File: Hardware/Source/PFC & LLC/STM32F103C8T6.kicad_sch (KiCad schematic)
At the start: 96 parts, among them J3 Conn_01x06_Socket, J4 Conn_01x02_Socket, J5 Conn_01x04_Pin, J6 Conn_01x05_Socket, Q6 LN2302LT1G, Q7 LN2302LT1G, Q8 LN2302LT1G, Q9 MMBT2222A, SW1 SW_Push, U10 ADS1115IDGS, U11 STM32F103C8T6, U12 MAX485CSA, Y1 Crystal_8MHz_SMD-4PIN

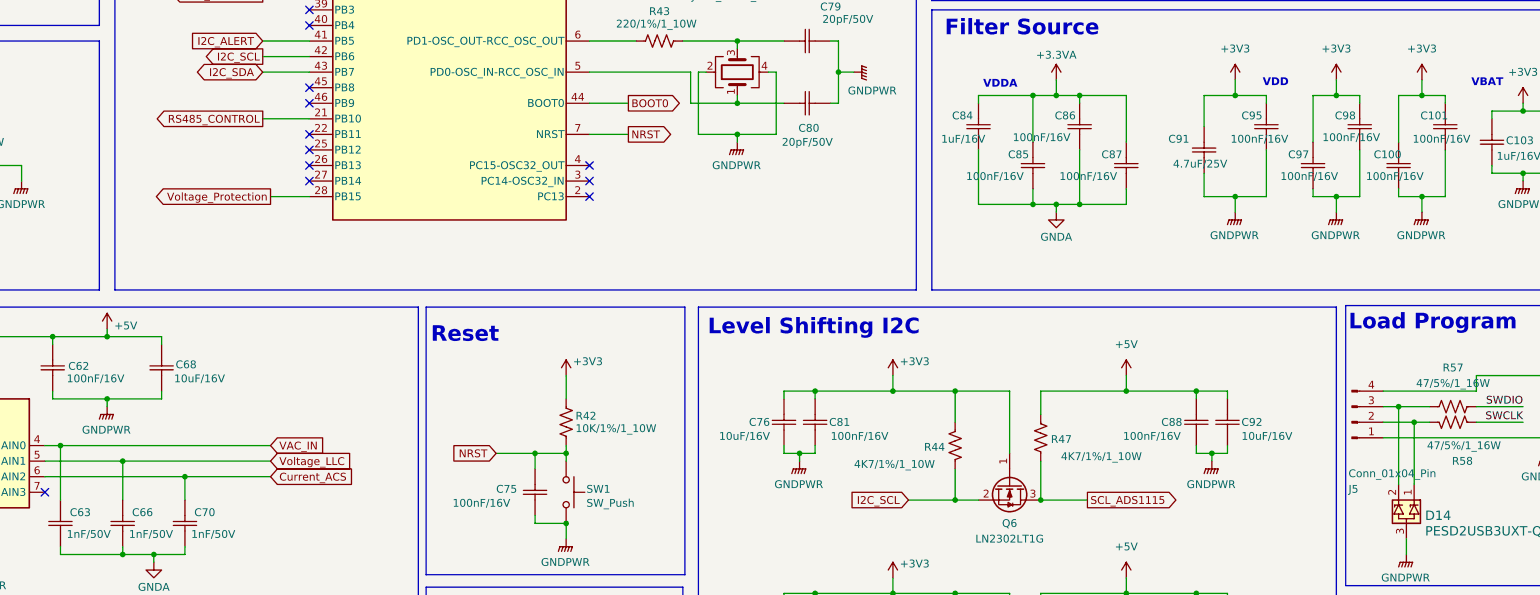
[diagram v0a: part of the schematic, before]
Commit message: Update PFC&LLC
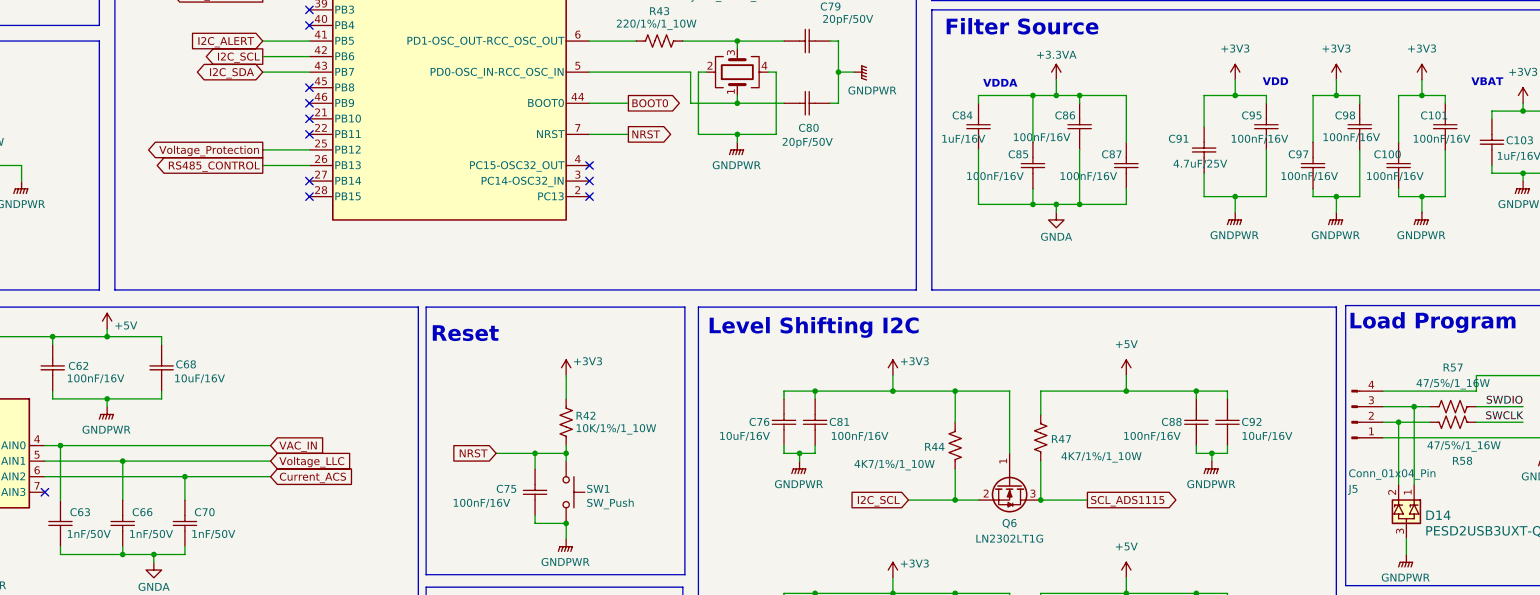
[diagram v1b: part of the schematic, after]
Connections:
- net RS485_CONTROL: now also U11.26 (PB13); no longer U11.21 (PB10)
- net Voltage_Protection: now also U11.25 (PB12); no longer U11.28 (PB15)
- net at J5.2 (Pin_2), R58.1: now also D14.2; no longer D14.1
- net at J5.3 (Pin_3), R57.1: now also D14.1; no longer D14.2
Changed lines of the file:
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@@
 	)
 	(junction
-		(at 293.37 160.02)
+		(at 295.91 160.02)
 		(diameter 0)
 		(color 0 0 0 0)
@@
 	)
 	(junction
+		(at 293.37 162.56)
+		(diameter 0)
+		(color 0 0 0 0)
+	)
+	(junction
 		(at 365.76 121.92)
 		(diameter 0)
@@
 	)
 	(junction
-		(at 295.91 162.56)
-		(diameter 0)
-		(color 0 0 0 0)
-	)
-	(junction
 		(at 307.34 73.66)
 		(diameter 0)
@@
 	)
 	(no_connect
-		(at 115.57 118.11)
-	)
-	(no_connect
-		(at 115.57 120.65)
-	)
-	(no_connect
 		(at 115.57 95.25)
 	)
@@
 	)
 	(no_connect
+		(at 115.57 125.73)
+	)
+	(no_connect
 		(at 115.57 115.57)
 	)
 	(no_connect
+		(at 115.57 113.03)
+	)
+	(no_connect
 		(at 161.29 125.73)
 	)
@@
 	(wire
 		(pts
+			(xy 295.91 160.02) (xy 298.45 160.02)
+		)
+		(stroke
+			(width 0)
+			(type default)
+		)
+	)
+	(wire
+		(pts
 			(xy 241.3 127) (xy 248.92 127)
 		)
@@
 	(wire
 		(pts
-			(xy 293.37 160.02) (xy 293.37 172.72)
+			(xy 260.35 200.66) (xy 260.35 199.39)
 		)
 		(stroke
@@
 	(wire
 		(pts
-			(xy 260.35 200.66) (xy 260.35 199.39)
+			(xy 234.95 232.41) (xy 234.95 238.76)
 		)
 		(stroke
@@
 	(wire
 		(pts
-			(xy 234.95 232.41) (xy 234.95 238.76)
+			(xy 293.37 162.56) (xy 293.37 172.72)
 		)
 		(stroke
@@
 	(wire
 		(pts
+			(xy 293.37 162.56) (xy 298.45 162.56)
+		)
+		(stroke
+			(width 0)
+			(type default)
+		)
+	)
+	(wire
+		(pts
 			(xy 347.98 116.84) (xy 368.3 116.84)
 		)
@@
 	(wire
 		(pts
-			(xy 109.22 125.73) (xy 115.57 125.73)
-		)
-		(stroke
-			(width 0)
-			(type default)
-		)
-	)
-	(wire
-		(pts
 			(xy 360.68 121.92) (xy 360.68 125.73)
 		)
@@
 	(wire
 		(pts
+			(xy 107.95 118.11) (xy 115.57 118.11)
+		)
+		(stroke
+			(width 0)
+			(type default)
+		)
+	)
+	(wire
+		(pts
 			(xy 321.31 40.64) (xy 321.31 45.72)
 		)
@@
 	(wire
 		(pts
+			(xy 295.91 160.02) (xy 295.91 172.72)
+		)
+		(stroke
+			(width 0)
+			(type default)
+		)
+	)
+	(wire
+		(pts
 			(xy 87.63 210.82) (xy 81.28 210.82)
 		)
@@
 	(wire
 		(pts
-			(xy 290.83 162.56) (xy 295.91 162.56)
-		)
-		(stroke
-			(width 0)
-			(type default)
-		)
-	)
-	(wire
-		(pts
 			(xy 363.22 110.49) (xy 363.22 119.38)
 		)
@@
 	(wire
 		(pts
+			(xy 107.95 120.65) (xy 115.57 120.65)
+		)
+		(stroke
+			(width 0)
+			(type default)
+		)
+	)
+	(wire
+		(pts
 			(xy 345.44 53.34) (xy 345.44 67.31)
 		)
@@
 	(wire
 		(pts
-			(xy 290.83 160.02) (xy 293.37 160.02)
+			(xy 290.83 160.02) (xy 295.91 160.02)
 		)
 		(stroke
@@
 	(wire
 		(pts
-			(xy 295.91 162.56) (xy 295.91 172.72)
-		)
-		(stroke
-			(width 0)
-			(type default)
-		)
-	)
-	(wire
-		(pts
 			(xy 107.95 87.63) (xy 115.57 87.63)
 		)
@@
 	(wire
 		(pts
-			(xy 293.37 160.02) (xy 298.45 160.02)
-		)
-		(stroke
-			(width 0)
-			(type default)
-		)
-	)
-	(wire
-		(pts
 			(xy 278.13 55.88) (xy 281.94 55.88)
 		)
@@
 	(wire
 		(pts
-			(xy 107.95 113.03) (xy 115.57 113.03)
-		)
-		(stroke
-			(width 0)
-			(type default)
-		)
-	)
-	(wire
-		(pts
 			(xy 38.1 120.65) (xy 40.64 120.65)
 		)
@@
 	(wire
 		(pts
-			(xy 295.91 162.56) (xy 298.45 162.56)
+			(xy 290.83 162.56) (xy 293.37 162.56)
 		)
 		(stroke
@@
 	(global_label "RS485_CONTROL"
 		(shape output)
-		(at 107.95 113.03 180)
+		(at 107.95 120.65 180)
 		(fields_autoplaced yes)
 		(effects
@@
 		)
 		(property "Intersheetrefs" "${INTERSHEET_REFS}"
-			(at 89.362 113.03 0)
+			(at 89.362 120.65 0)
 			(effects
 				(font
@@
 	(global_label "Voltage_Protection"
 		(shape output)
-		(at 109.22 125.73 180)
+		(at 107.95 118.11 180)
 		(fields_autoplaced yes)
 		(effects
@@
 		)
 		(property "Intersheetrefs" "${INTERSHEET_REFS}"
-			(at 88.5155 125.73 0)
+			(at 87.2455 118.11 0)
 			(effects
 				(font

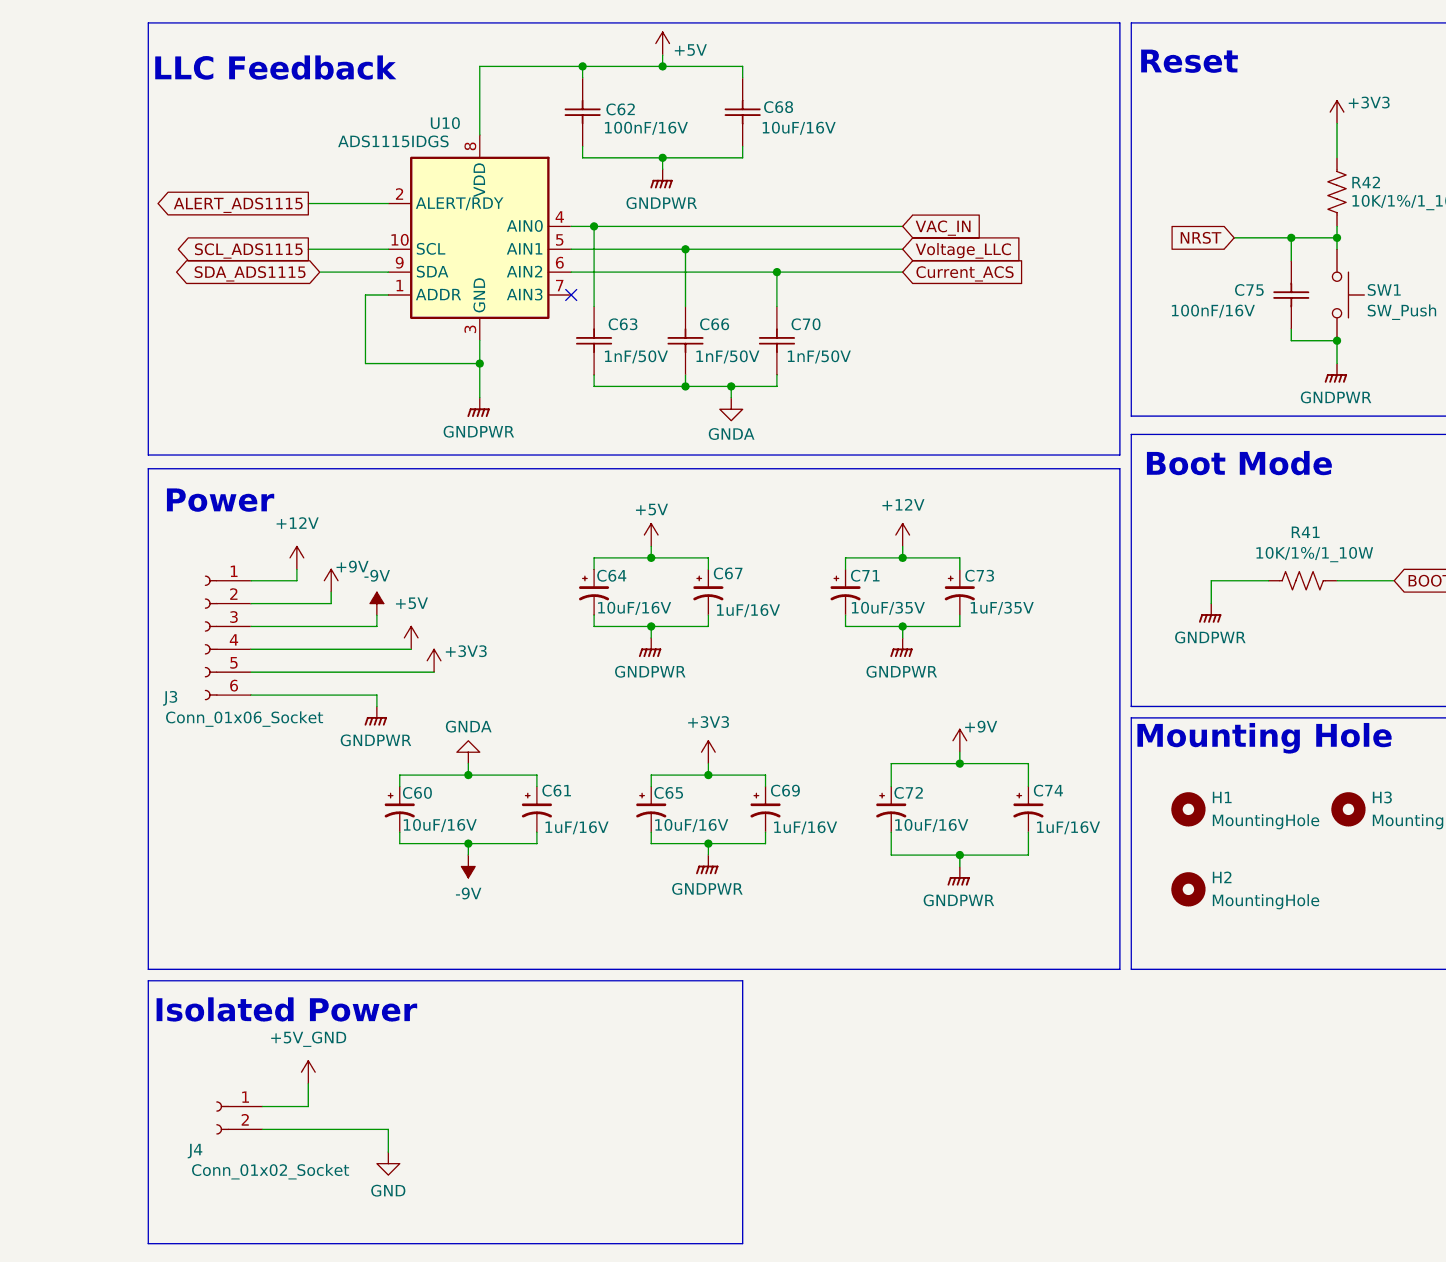
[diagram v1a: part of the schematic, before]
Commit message: Update PFC&LLC
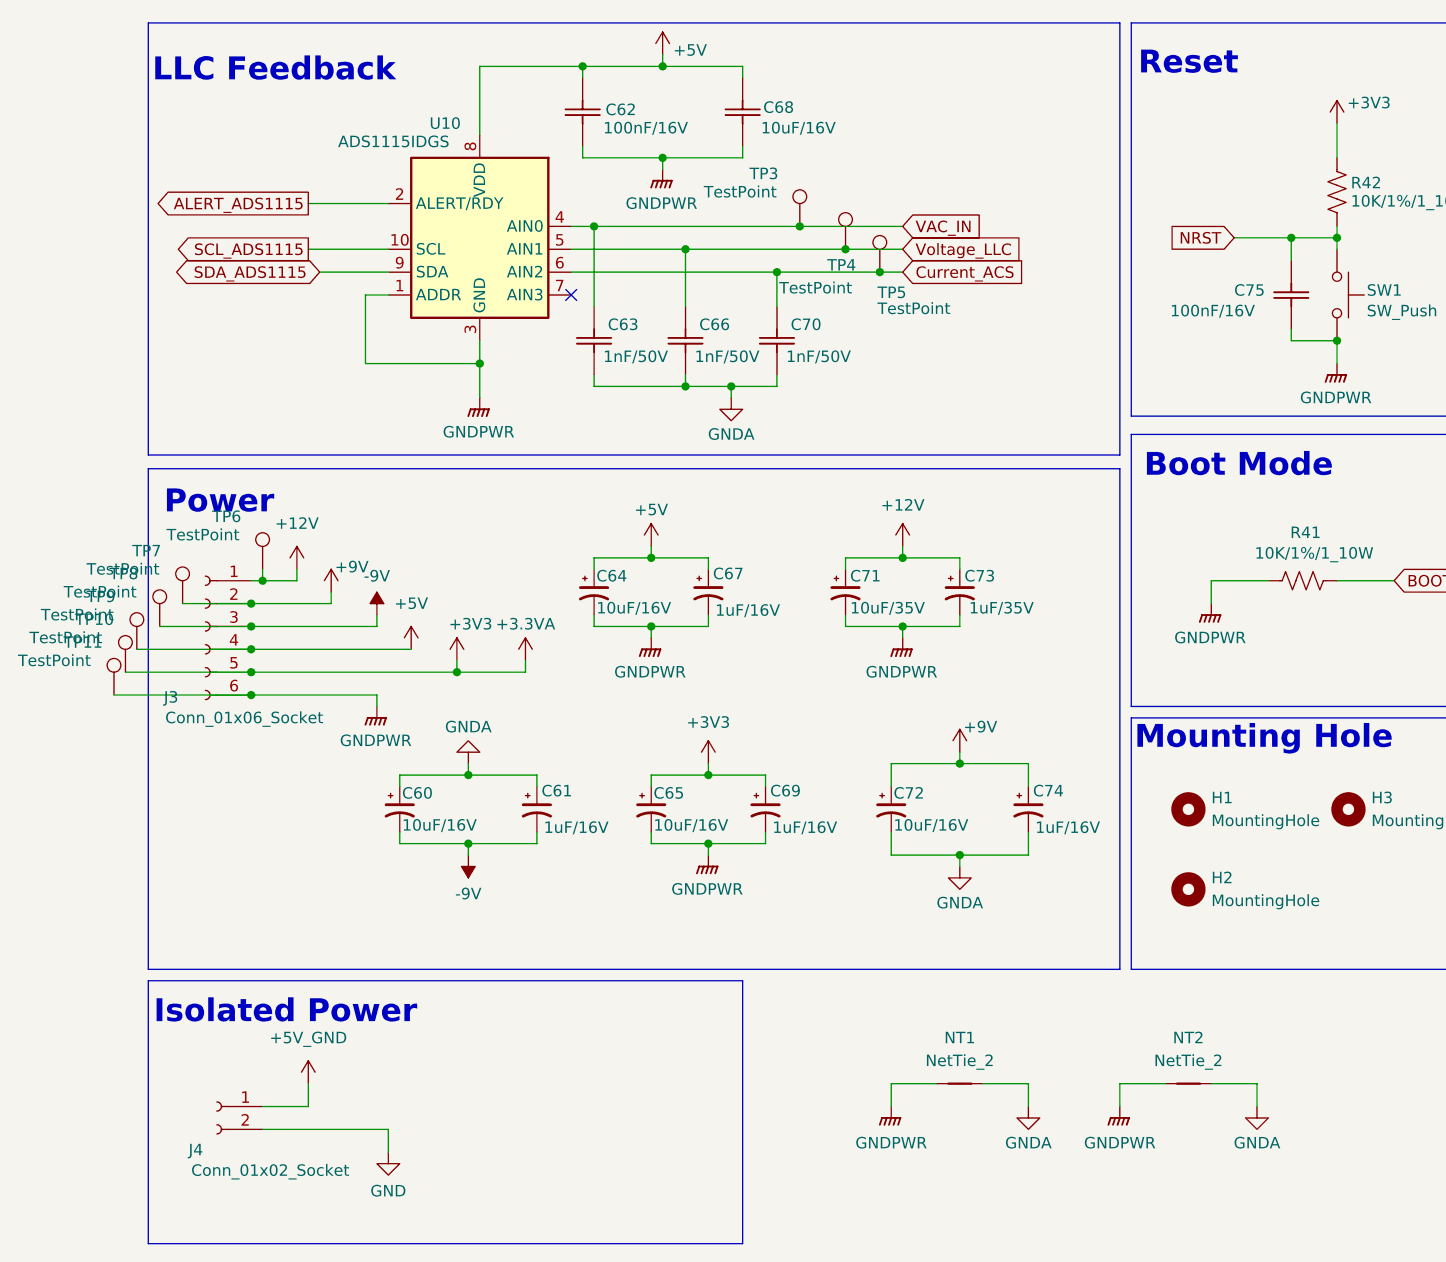
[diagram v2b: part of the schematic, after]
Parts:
- added NT1, NT2: NetTie_2, NetTie:NetTie-2_SMD_Pad0.5mm, symbol Device:NetTie_2
- added TP10, TP11, TP3, TP4, TP5, TP6, TP7, TP8, TP9: TestPoint, TestPoint:TestPoint_Pad_D1.0mm, symbol Connector:TestPoint
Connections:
- net +3V3 is gone; now on net +3.3VA: C100.2, C101.2, C102.2, C103.2, C104.2, C105.2, C65.1, C69.1, C76.2, C77.2, C78.2, C81.2, C82.2, C83.2, C91.2, C95.2, C97.2, C98.2, J3.5 (Pin_5), J5.4 (Pin_4), Q6.1 (G), Q7.1 (G), Q8.1 (G), R42.2, R44.2, R45.2, R46.2, R50.2, R52.1, R53.2, R54.2, R62.2, R63.2, U11.1 (VBAT), U11.24 (VDD_1), U11.36 (VDD_2), U11.48 (VDD_3)
- net +12V: now also TP6.1
- net +3.3VA: now also TP10.1
- net +5V: now also TP9.1
- net +9V: now also TP7.1
- net -9V: now also TP8.1
- net Current_ACS: now also TP5.1
- net GNDA: now also C72.2, C74.2, NT1.2, NT2.2
- net GNDPWR: now also NT1.1, NT2.1, TP11.1; no longer C72.2, C74.2
- net VAC_IN: now also TP3.1
- net Voltage_LLC: now also TP4.1

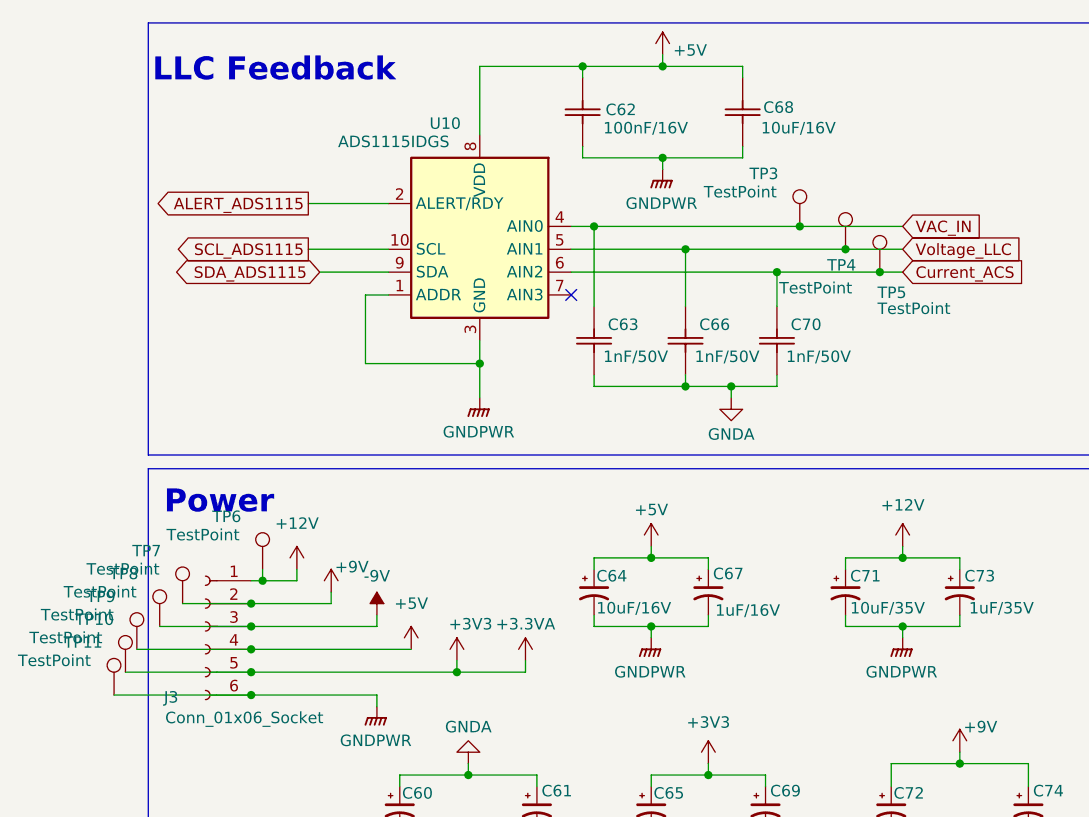
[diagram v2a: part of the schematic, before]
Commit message: Update PFC&LLC
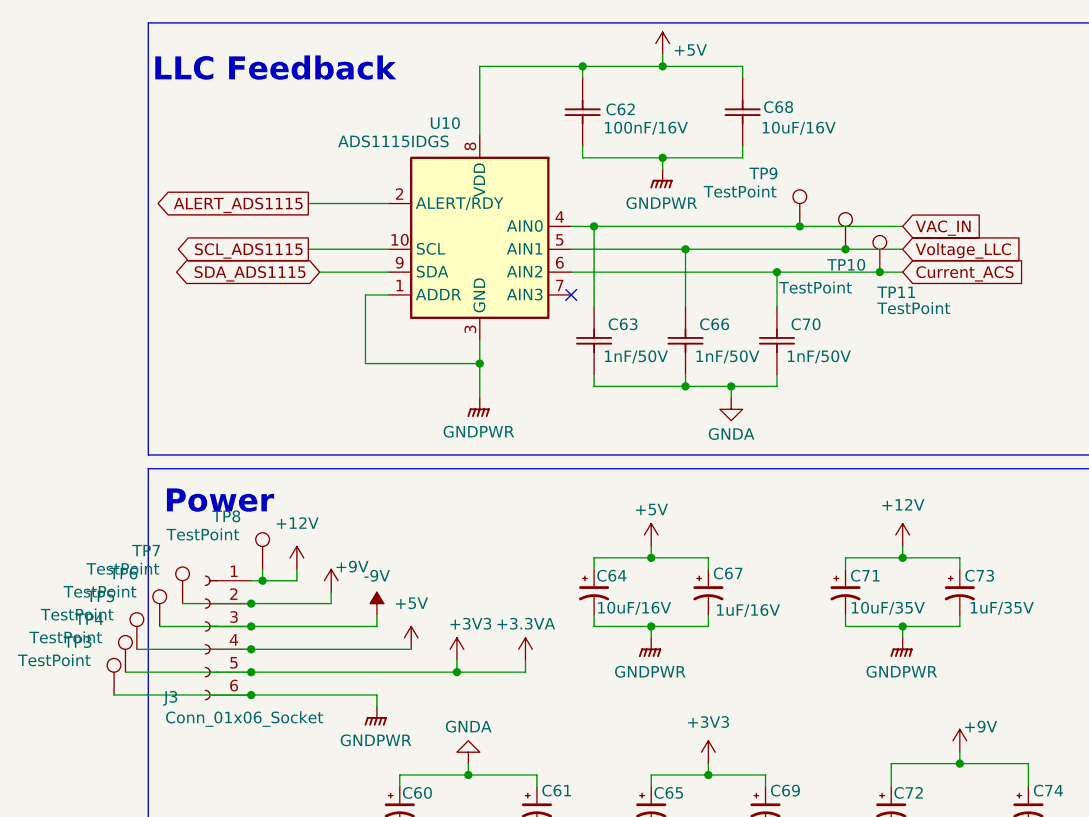
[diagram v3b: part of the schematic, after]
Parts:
- renumbered TP4 to TP10, TP5 to TP11, TP11 to TP3, TP10 to TP4, TP9 to TP5, TP8 to TP6, TP6 to TP8, TP3 to TP9
